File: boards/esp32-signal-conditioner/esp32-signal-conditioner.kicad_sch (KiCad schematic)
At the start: 5 parts

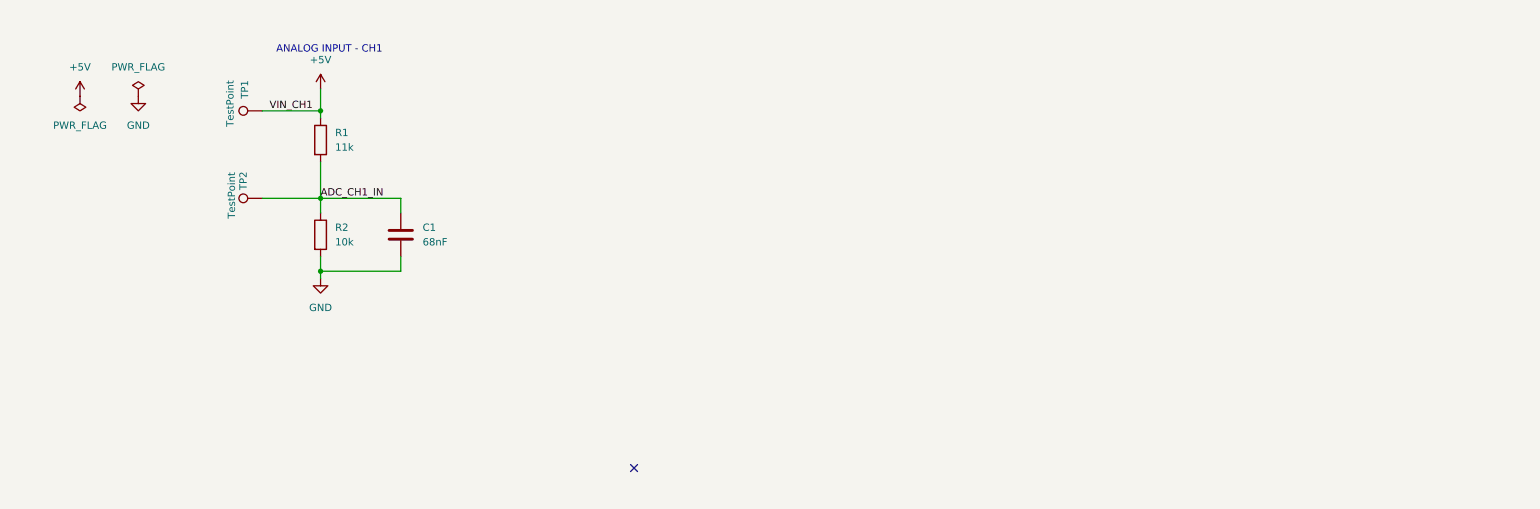
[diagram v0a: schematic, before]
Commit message: Add J1 input connector TBL002A 5-pos 3.5mm, footprint assigned, ERC clean
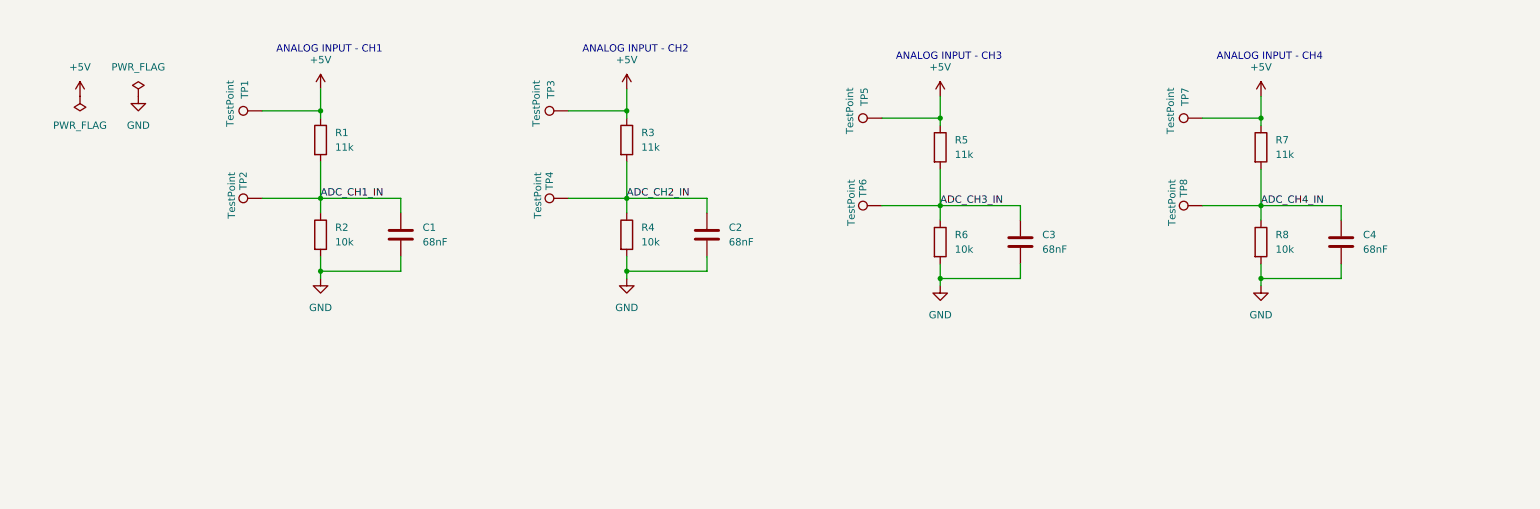
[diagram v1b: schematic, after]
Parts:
- added C2, C3, C4: 68nF, symbol Device:C
- added R3, R5, R7: 11k, symbol Device:R
- added R4, R6, R8: 10k, symbol Device:R
- added TP3, TP4, TP5, TP6, TP7, TP8: TestPoint, symbol Connector:TestPoint
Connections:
- net +5V: now also R3.1, R5.1, R7.1, TP3.1, TP5.1, TP7.1
- net GND: now also C2.2, C3.2, C4.2, R4.2, R6.2, R8.2
- new net ADC_CH2_IN: C2.1, R3.2, R4.1, TP4.1
- new net ADC_CH3_IN: C3.1, R5.2, R6.1, TP6.1
- new net ADC_CH4_IN: C4.1, R7.2, R8.1, TP8.1
- no-connect marks 1 -> 0
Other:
- note added: "ANALOG INPUT - CH2"
- note added: "ANALOG INPUT - CH3"
- note added: "ANALOG INPUT - CH4"

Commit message: Add C5 100nF and C6 10uF decoupling on +5V rail, ERC clean
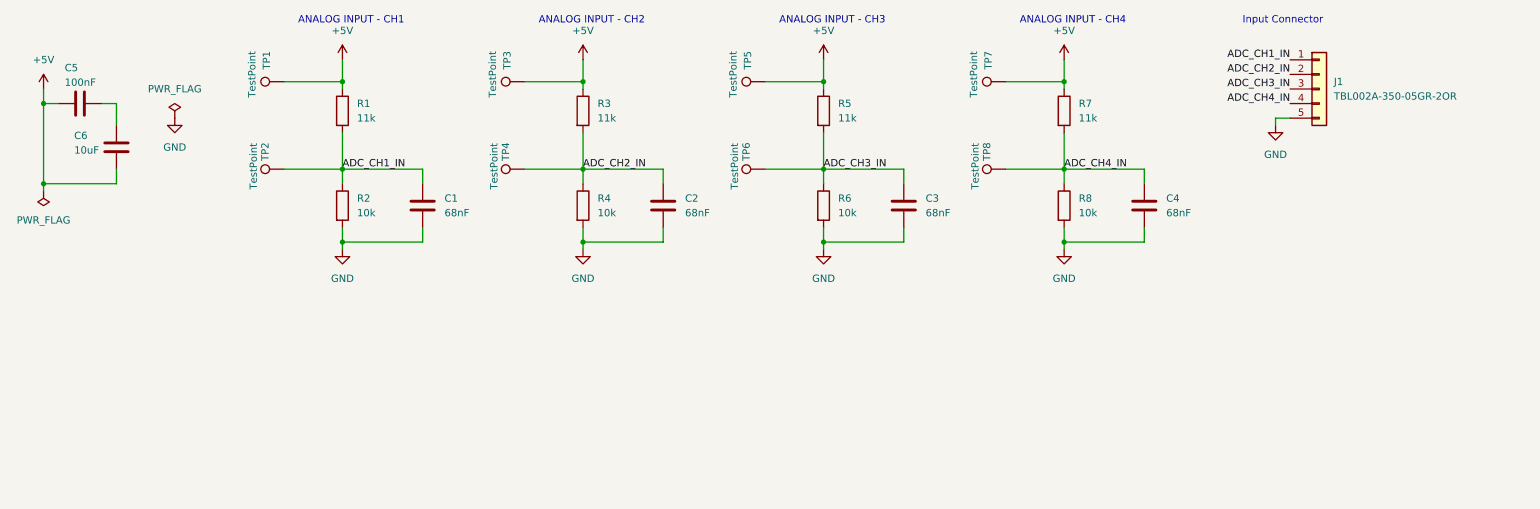
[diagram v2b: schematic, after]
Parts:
- added C5: 100nF, symbol Device:C
- added C6: 10uF, symbol Device:C
- added J1: TBL002A-350-05GR-2OR, TerminalBlock_Degson:TerminalBlock_Degson_DG250-3.5-05P_1x05_P3.50mm_45Degree, symbol Connector_Generic:Conn_01x05
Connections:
- net +5V: now also C5.1, C6.2
- net ADC_CH1_IN: now also J1.1 (Pin_1)
- net ADC_CH2_IN: now also J1.2 (Pin_2)
- net ADC_CH3_IN: now also J1.3 (Pin_3)
- net ADC_CH4_IN: now also J1.4 (Pin_4)
- net GND: now also J1.5 (Pin_5)
- new net: C5.2, C6.1
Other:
- note added: "Input Connector"
- moved on the sheet: C1, C2, C3, C4, R1, R2, R3, R4, R5, R6, R7, R8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

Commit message: Add AP2112k-3.3 LDO power regulation, C7 C8 decoupling, ERC clean
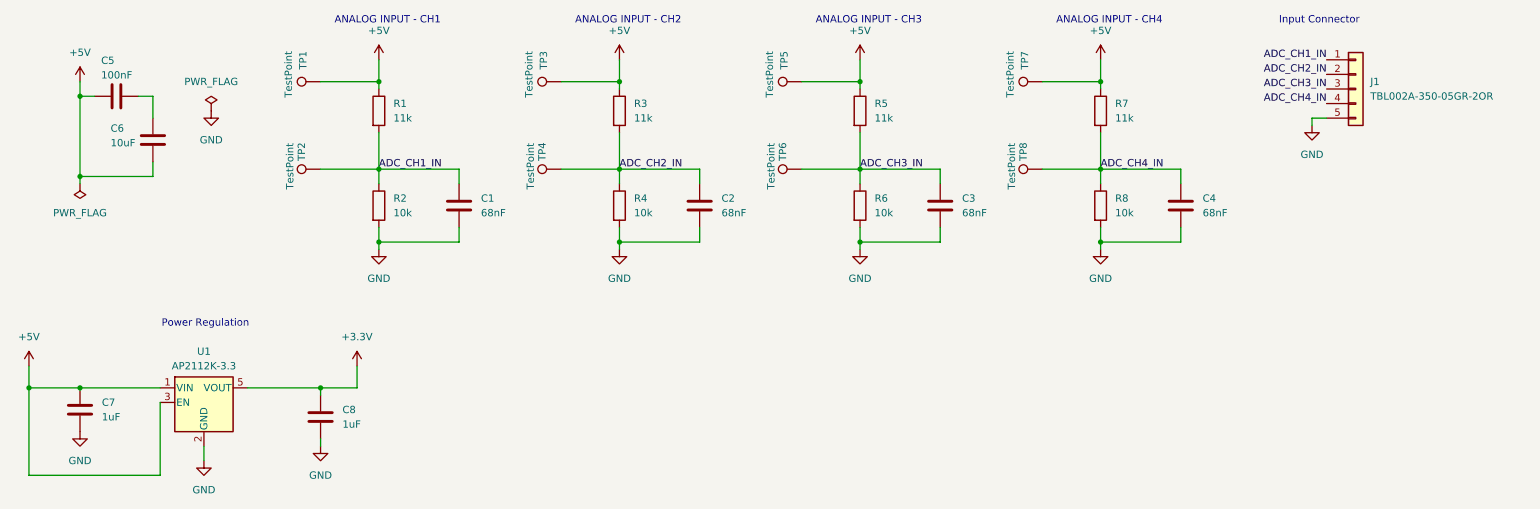
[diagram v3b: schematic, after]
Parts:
- added C7, C8: 1uF, symbol Device:C
- added U1: AP2112K-3.3, Package_TO_SOT_SMD:SOT-23-5, symbol Regulator_Linear:AP2112K-3.3
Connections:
- net +5V: now also C7.1, U1.1 (VIN), U1.3 (EN)
- net GND: now also C7.2, C8.2, U1.2 (GND)
- new net +3.3V: C8.1, U1.5 (VOUT)
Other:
- note added: "Power Regulation"
- moved on the sheet: C1, C2, C3, C4, C5, C6, J1, R1, R2, R3, R4, R5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
